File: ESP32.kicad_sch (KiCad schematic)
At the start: 37 parts, among them J1 Debug_U0, J16 USB_NATIVO, J3 USB_UART0, J4 Uart1, Q3 SS8050, Q4 SS8050, U3 CP2102N-A02-GQFN24, U8 ESP32-S3-WROOM-1

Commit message: routing
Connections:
- net USB2_DM renamed USB2_D-
- net USB2_DP renamed USB2_D+
- net USB_DM renamed USB_D-
- net USB_DP renamed USB_D+
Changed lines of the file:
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@@
 	)
 	(junction
+		(at 167.64 71.12)
+		(diameter 0)
+		(color 0 0 0 0)
+	)
+	(junction
 		(at 245.11 116.84)
 		(diameter 0)
@@
 	)
 	(junction
-		(at 167.64 71.12)
-		(diameter 0)
-		(color 0 0 0 0)
-	)
-	(junction
 		(at 265.43 46.99)
 		(diameter 0)
@@
 		)
 	)
-	(label "USB2_DM"
+	(label "USB2_D-"
 		(at 267.97 152.4 0)
 		(effects
@@
 		)
 	)
-	(label "USB2_DM"
+	(label "USB2_D-"
 		(at 99.06 137.16 0)
 		(effects
@@
 		)
 	)
-	(label "USB_DM"
+	(label "USB_D-"
 		(at 69.85 62.23 180)
 		(effects
@@
 		)
 	)
-	(label "USB_DP"
+	(label "USB_D+"
 		(at 205.74 66.04 0)
 		(effects
@@
 		)
 	)
-	(label "USB_DM"
+	(label "USB_D-"
 		(at 185.42 48.26 0)
 		(effects
@@
 		)
 	)
-	(label "USB2_DM"
+	(label "USB2_D-"
 		(at 247.65 132.08 0)
 		(effects
@@
 		)
 	)
-	(label "USB2_DP"
+	(label "USB2_D+"
 		(at 247.65 137.16 0)
 		(effects
@@
 		)
 	)
-	(label "USB2_DP"
+	(label "USB2_D+"
 		(at 267.97 149.86 0)
 		(effects
@@
 		)
 	)
-	(label "USB_DP"
+	(label "USB_D+"
 		(at 185.42 53.34 0)
 		(effects
@@
 		)
 	)
-	(label "USB_DM"
+	(label "USB_D-"
 		(at 205.74 68.58 0)
 		(effects
@@
 		)
 	)
-	(label "USB2_DP"
+	(label "USB2_D+"
 		(at 99.06 139.7 0)
 		(effects
@@
 		)
 	)
-	(label "USB_DP"
+	(label "USB_D+"
 		(at 69.85 64.77 180)
 		(effects
@@
 		(lib_id "power:+3.3V")
 		(at 45.72 46.99 90)
+		(mirror x)
 		(unit 1)
 		(body_style 1)
@@
 		(in_pos_files yes)
 		(dnp no)
-		(fields_autoplaced yes)
 		(property "Reference" "#PWR031"
 			(at 49.53 46.99 0)
@@
 		)
 		(property "Value" "CP2102_3V3"
-			(at 44.45 44.45 90)
+			(at 44.45 49.53 90)
 			(show_name no)
 			(do_not_autoplace no)
@@
 		(in_pos_files yes)
 		(dnp no)
-		(fields_autoplaced yes)
 		(property "Reference" "J3"
 			(at 167.64 25.4 0)

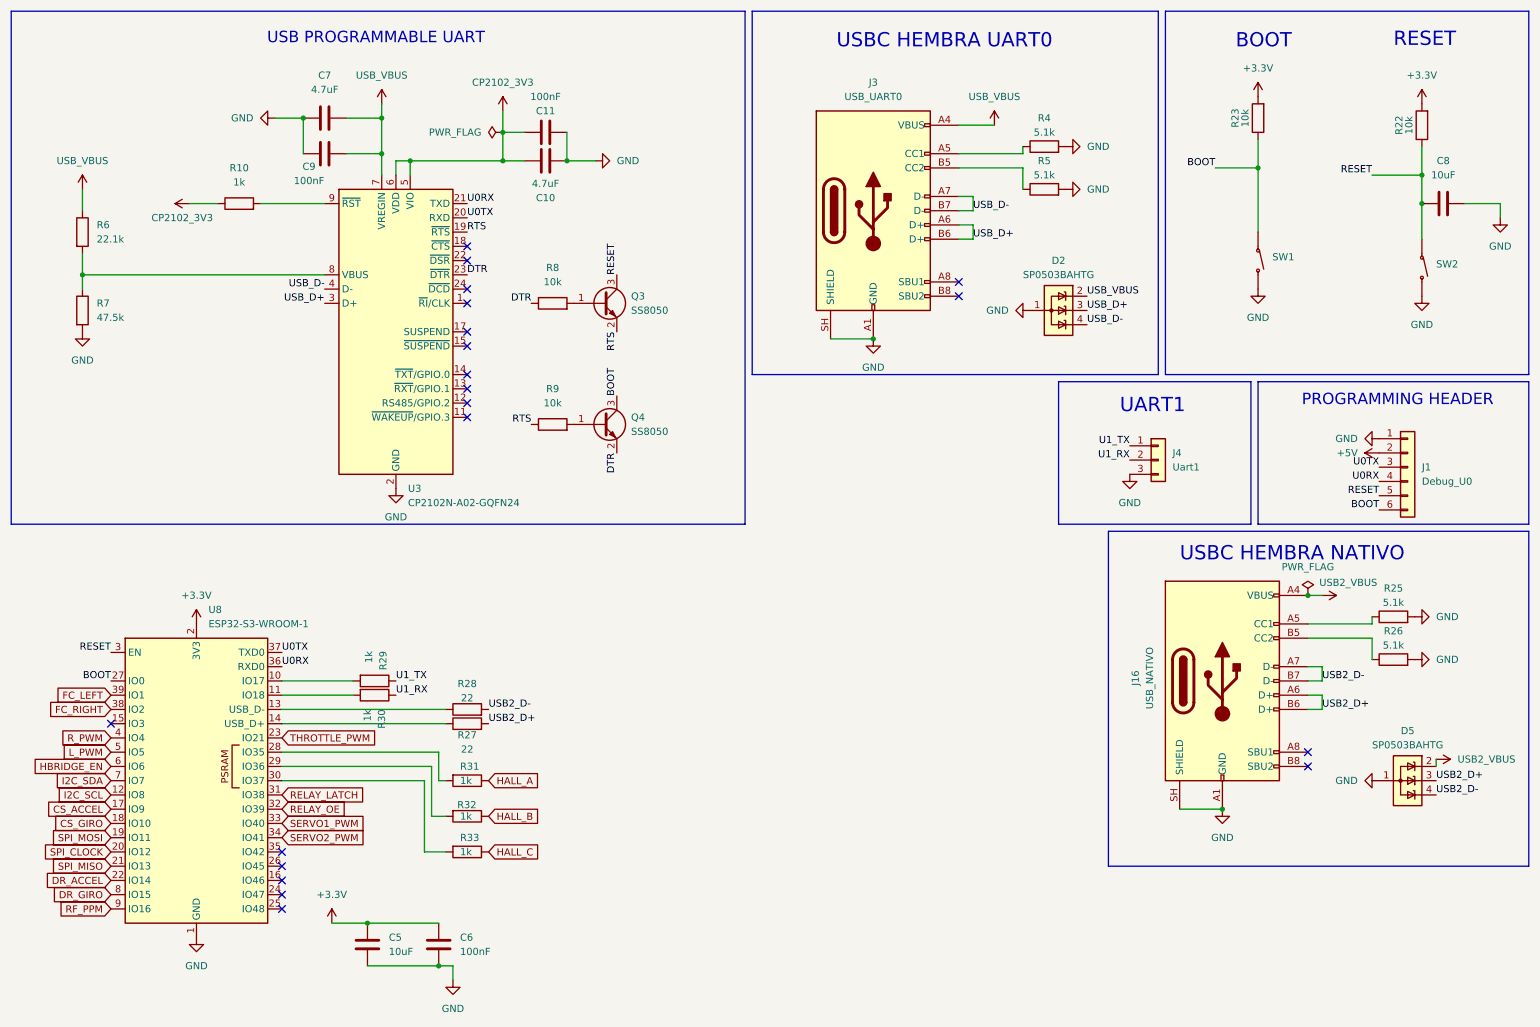
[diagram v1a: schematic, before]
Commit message: removed usb_uart0
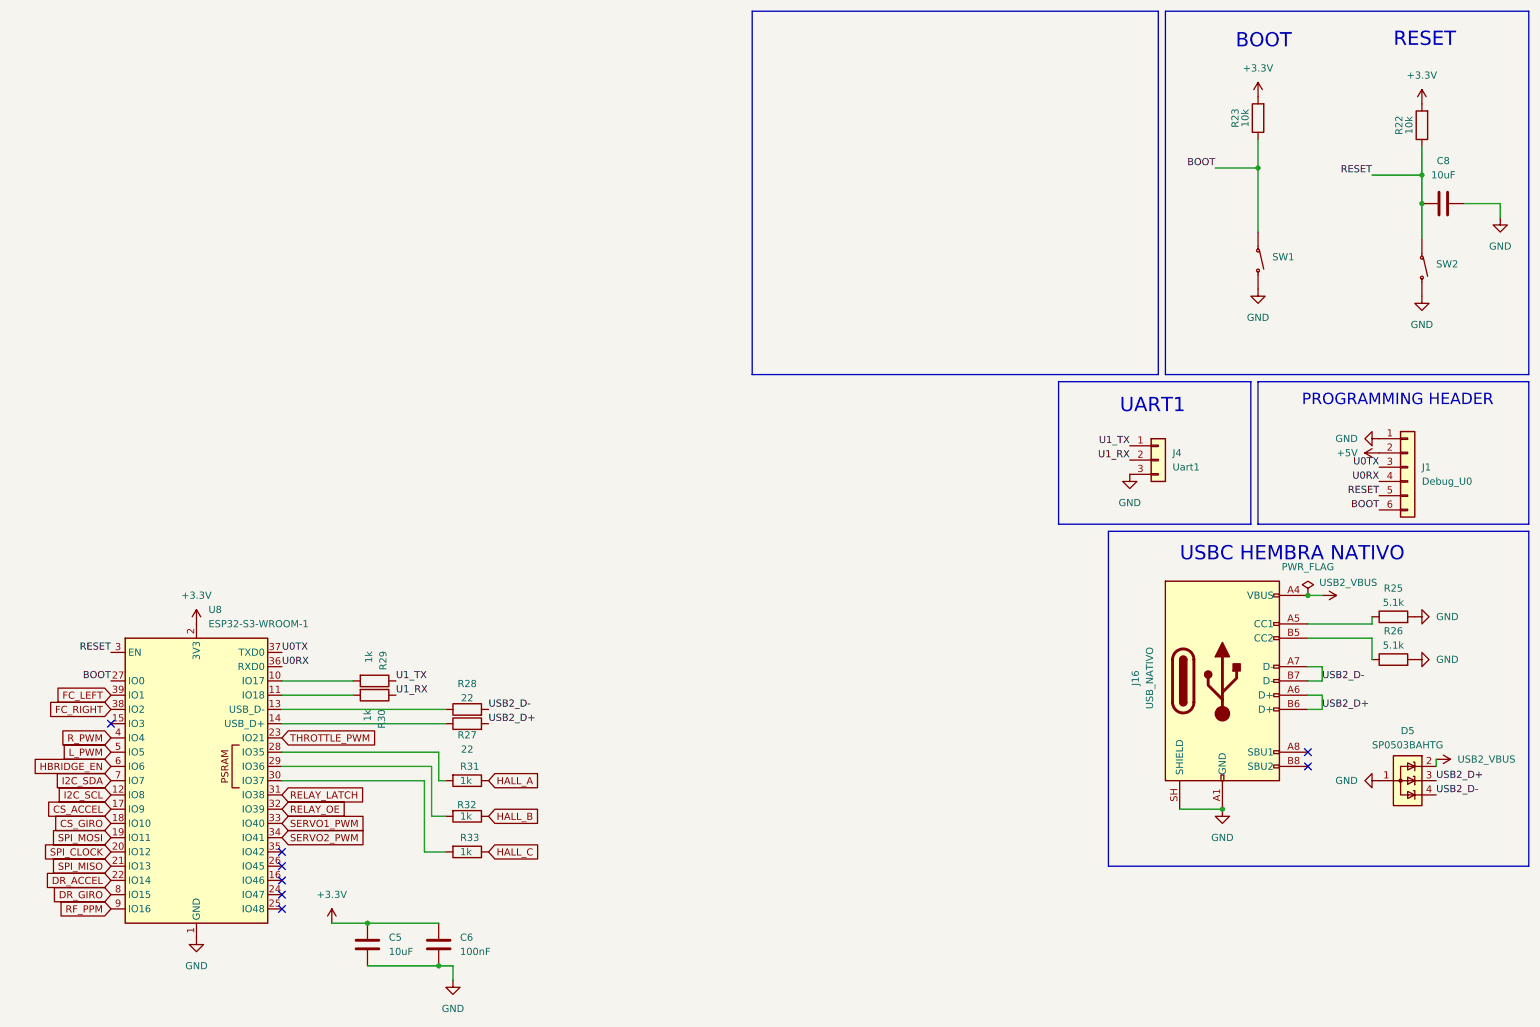
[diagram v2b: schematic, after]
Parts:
- removed C10, C7: 4.7uF, Capacitor_SMD:C_0805_2012Metric, symbol Device:C
- removed C11, C9: 100nF, Capacitor_SMD:C_0603_1608Metric, symbol Device:C
- removed D2: SP0503BAHTG, Package_TO_SOT_SMD:SOT-143, symbol Power_Protection:SP0503BAHT
- removed J3: USB_UART0, Connector_USB:USB_C_Receptacle_G-Switch_GT-USB-7010ASV, symbol Connector:USB_C_Receptacle_USB2.0_16P
- removed Q3, Q4: SS8050, Package_TO_SOT_SMD:SOT-23, symbol Transistor_BJT:SS8050
- removed R10: 1k, Resistor_SMD:R_0603_1608Metric, symbol Device:R
- removed R4, R5: 5.1k, Resistor_SMD:R_0603_1608Metric, symbol Device:R
- removed R6: 22.1k, Resistor_SMD:R_0603_1608Metric, symbol Device:R
- removed R7: 47.5k, Resistor_SMD:R_0603_1608Metric, symbol Device:R
- removed R8, R9: 10k, Resistor_SMD:R_0603_1608Metric, symbol Device:R
- removed U3: CP2102N-A02-GQFN24, Package_DFN_QFN:QFN-24-1EP_4x4mm_P0.5mm_EP2.6x2.6mm, symbol Interface_USB:CP2102N-Axx-xQFN24
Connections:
- no-connect marks 20 -> 8
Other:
- note removed: "USB PROGRAMMABLE UART"
- note removed: "USBC HEMBRA UART0"

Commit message: fixes
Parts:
- SW1, SW2: footprint Footprints:Boton_Simple -> Footprints:Switch-Definitivo; LCSC PN C36936655 -> C318884; MPN TS1201-TZ25HAM -> TS-1187A-B-A-B; Manufacturer BXCONN(宝讯) -> XKB Connection; Manufacturer Part TS1201-TZ25HAM -> TS-1187A-B-A-B; Supplier Part C36936655 -> C318884
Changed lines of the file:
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@@
 			)
 		)
-		(property "Footprint" "Footprints:Boton_Simple"
+		(property "Footprint" "Footprints:Switch-Definitivo"
 			(at 236.22 57.15 0)
 			(hide yes)
@@
 			)
 		)
-		(property "Datasheet" "https://atta.szlcsc.com/upload/public/pdf/source/20240731/528267057C6169D47FE6AADDB119A0E9.pdf"
+		(property "Datasheet" "http://www.helloxkb.com/uploads/qingchukaiguan/TS-1187A-X-X-X.pdf"
 			(at 236.22 57.15 0)
 			(hide yes)
@@
 			)
 		)
-		(property "Manufacturer Part" "TS1201-TZ25HAM"
+		(property "Manufacturer Part" "TS-1187A-B-A-B"
 			(at 236.22 57.15 0)
 			(hide yes)
@@
 			)
 		)
-		(property "Manufacturer" "BXCONN(宝讯)"
+		(property "Manufacturer" "XKB Connection"
 			(at 236.22 57.15 0)
 			(hide yes)
@@
 			)
 		)
-		(property "Supplier Part" "C36936655"
+		(property "Supplier Part" "C318884"
 			(at 236.22 57.15 0)
 			(hide yes)
@@
 			)
 		)
-		(property "LCSC PN" "C36936655"
+		(property "LCSC PN" "C318884"
 			(at 236.22 57.15 90)
 			(hide yes)
@@
 			)
 		)
-		(property "MPN" "TS1201-TZ25HAM"
+		(property "MPN" "TS-1187A-B-A-B"
 			(at 0 0 0)
 			(hide yes)
@@
 			)
 		)
-		(property "Footprint" "Footprints:Boton_Simple"
+		(property "Footprint" "Footprints:Switch-Definitivo"
 			(at 265.43 58.42 0)
 			(hide yes)
@@
 			)
 		)
-		(property "Datasheet" "https://atta.szlcsc.com/upload/public/pdf/source/20240731/528267057C6169D47FE6AADDB119A0E9.pdf"
+		(property "Datasheet" "http://www.helloxkb.com/uploads/qingchukaiguan/TS-1187A-X-X-X.pdf"
 			(at 265.43 58.42 0)
 			(hide yes)
@@
 			)
 		)
-		(property "Manufacturer Part" "TS1201-TZ25HAM"
+		(property "Manufacturer Part" "TS-1187A-B-A-B"
 			(at 265.43 58.42 0)
 			(hide yes)
@@
 			)
 		)
-		(property "Manufacturer" "BXCONN(宝讯)"
+		(property "Manufacturer" "XKB Connection"
 			(at 265.43 58.42 0)
 			(hide yes)
@@
 			)
 		)
-		(property "Supplier Part" "C36936655"
+		(property "Supplier Part" "C318884"
 			(at 265.43 58.42 0)
 			(hide yes)
@@
 			)
 		)
-		(property "LCSC PN" "C36936655"
+		(property "LCSC PN" "C318884"
 			(at 265.43 58.42 90)
 			(hide yes)
@@
 			)
 		)
-		(property "MPN" "TS1201-TZ25HAM"
+		(property "MPN" "TS-1187A-B-A-B"
 			(at 0 0 0)
 			(hide yes)
